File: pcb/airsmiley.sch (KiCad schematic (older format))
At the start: 12 parts, among them J1 Conn_01x02, U1 WeMos_D1_mini

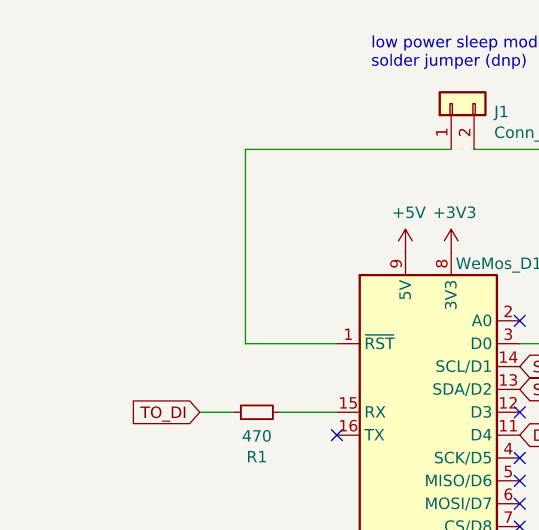
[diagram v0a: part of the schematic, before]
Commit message: Renamed to "Air Smiley"
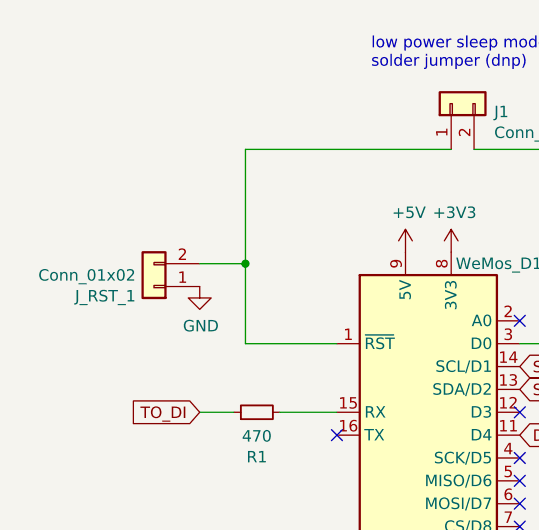
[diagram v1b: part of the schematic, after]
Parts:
- added J_RST_1: Conn_01x02, Connector_PinHeader_2.54mm:PinHeader_1x02_P2.54mm_Vertical, symbol Connector_Generic:Conn_01x02
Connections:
- net GND: now also J_RST_1.1 (Pin_1)
- net at J1.1 (Pin_1), U1.1 (~RST): now also J_RST_1.2 (Pin_2)
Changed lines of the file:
@@
 encoding utf-8
 Sheet 1 1
-Title "CO2box"
-Date "2020-11-27"
-Rev "v0"
-Comp "Christoph B. Wurzinger"
-Comment1 ""
+Title "Air Smiley"
+Date "2021-02-13"
+Rev "v1"
+Comp "HTL Weiz"
+Comment1 "Christoph B. Wurzinger"
 Comment2 ""
 Comment3 ""
@@
 	4350 2300 3600 2300
 Wire Wire Line
-	2600 2300 2600 3150
+	2600 2300 2600 2800
 Wire Wire Line
 	2600 3150 3000 3150
@@
 NoConn ~ 3800 3450
 NoConn ~ 3800 3050
+$Comp
+L Connector_Generic:Conn_01x02 J_RST_1
+U 1 1 6027AC57
+P 2200 2900
+F 0 "J_RST_1" H 2280 2942 50  0000 L CNN
+F 1 "Conn_01x02" H 2280 2851 50  0000 L CNN
+F 2 "Connector_PinHeader_2.54mm:PinHeader_1x02_P2.54mm_Vertical" H 2200 2900 50  0001 C CNN
+F 3 "~" H 2200 2900 50  0001 C CNN
+	1    2200 2900
+	-1   0    0    1
+$EndComp
+$Comp
+L power:GND #PWR01
+U 1 1 6027CA7F
+P 2400 2900
+F 0 "#PWR01" H 2400 2650 50  0001 C CNN
+F 1 "GND" H 2405 2727 50  0000 C CNN
+F 2 "" H 2400 2900 50  0001 C CNN
+F 3 "" H 2400 2900 50  0001 C CNN
+	1    2400 2900
+	1    0    0    -1
+$EndComp
+Wire Wire Line
+	2400 2800 2600 2800
+Connection ~ 2600 2800
+Wire Wire Line
+	2600 2800 2600 3150
 $EndSCHEMATC
